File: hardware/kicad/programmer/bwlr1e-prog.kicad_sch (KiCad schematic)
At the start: 46 parts, among them J1 DEBUG, J2 USB_C_Receptacle_USB2.0, J3 RESET, J4 BOOT, Q1 AO3407A, SW1 SW_DIP_x04, SW4 BOOT, SW5 RESET, U1 USBLC6-2P6, U6 CH340E, U7 MCP73831T-2ACI/OT, U8 XC6220B331MR-G

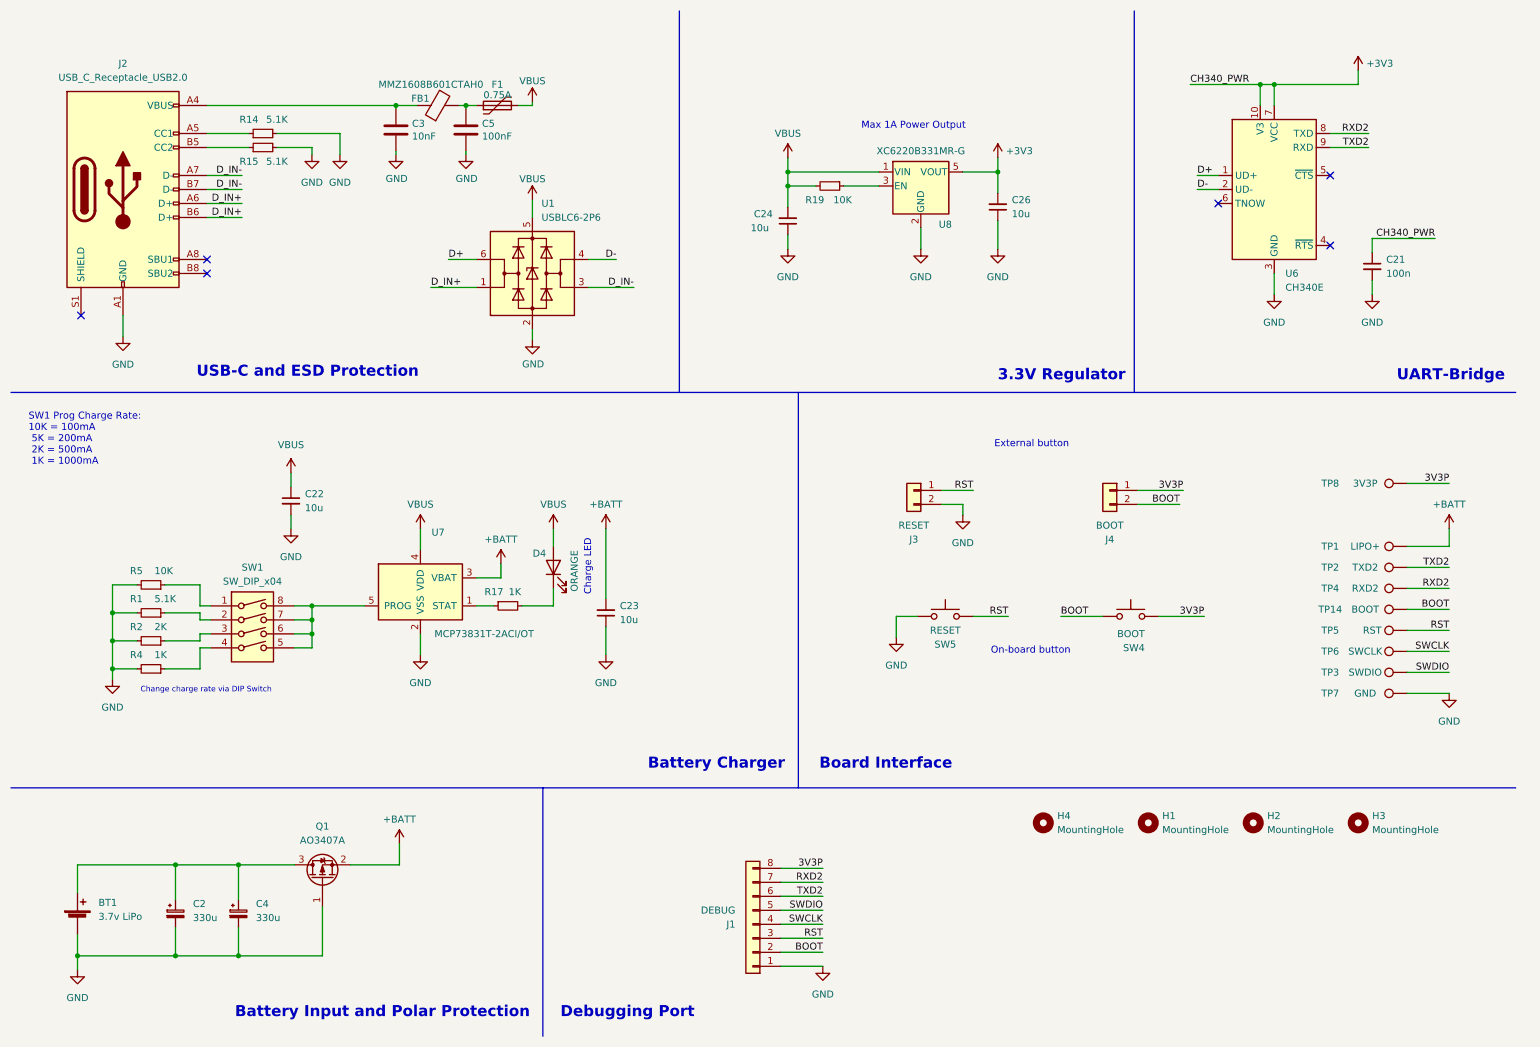
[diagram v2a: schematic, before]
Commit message: fix components value
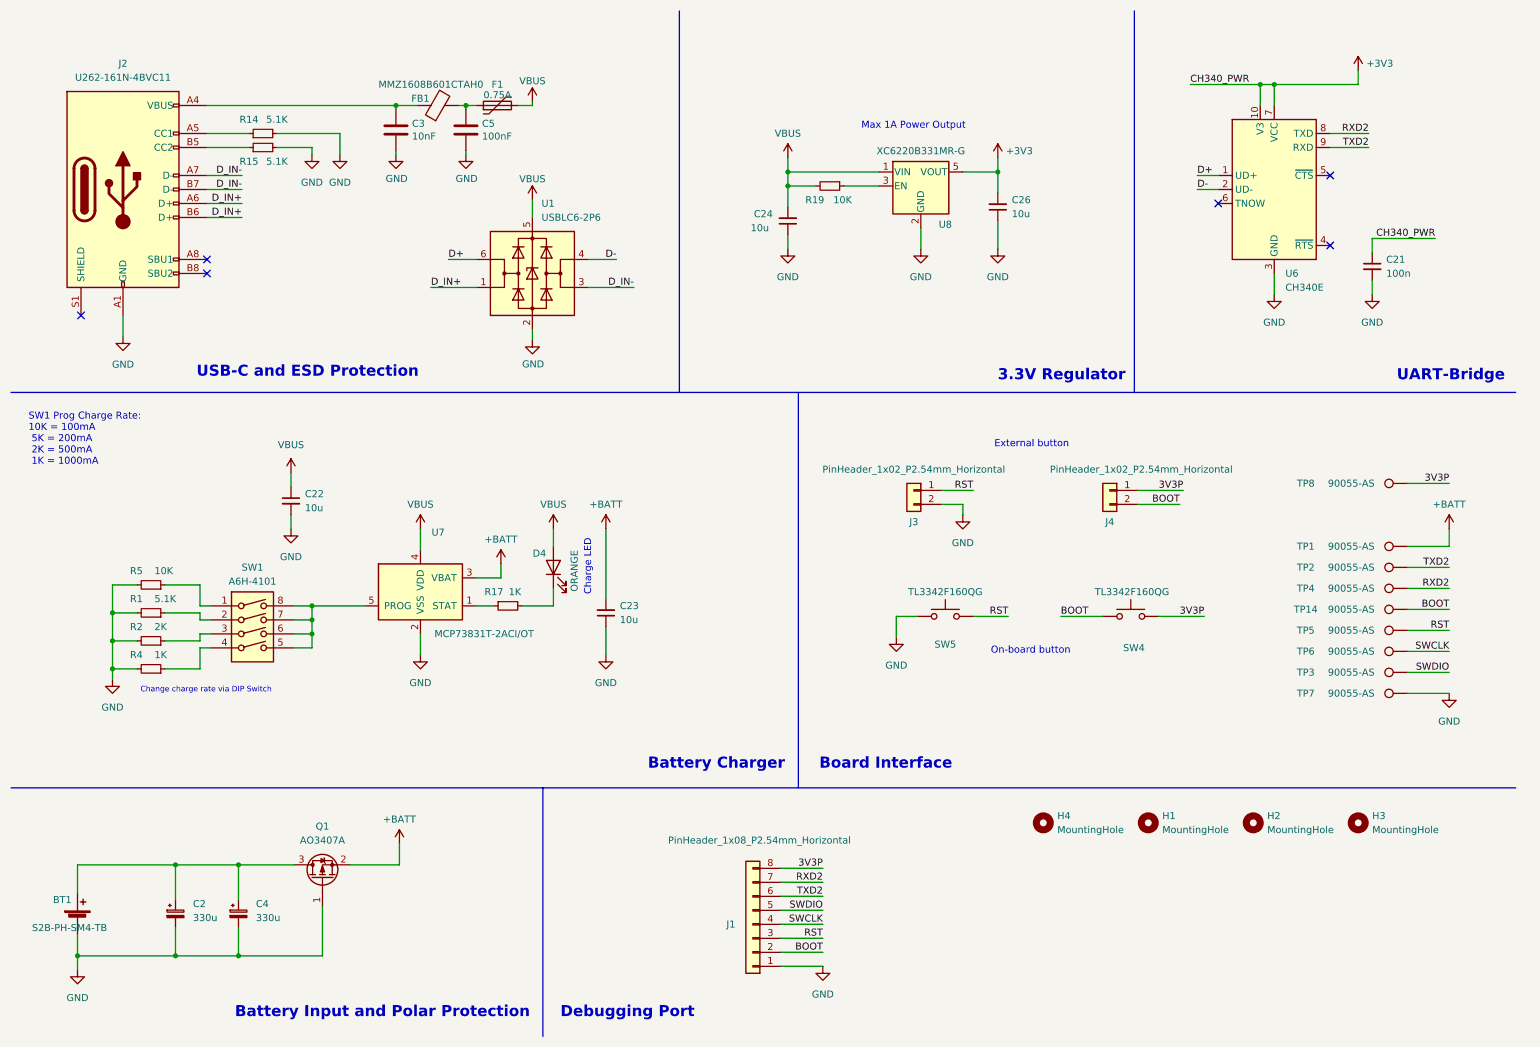
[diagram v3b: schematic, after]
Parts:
- BT1: value 3.7v LiPo -> S2B-PH-SM4-TB
- J1: value DEBUG -> PinHeader_1x08_P2.54mm_Horizontal
- J2: value USB_C_Receptacle_USB2.0 -> U262-161N-4BVC11
- J3: value RESET -> PinHeader_1x02_P2.54mm_Horizontal
- J4: value BOOT -> PinHeader_1x02_P2.54mm_Horizontal
- SW1: value SW_DIP_x04 -> A6H-4101
- SW4: value BOOT -> TL3342F160QG
- SW5: value RESET -> TL3342F160QG
- TP1: value LIPO+ -> 90055-AS
- TP14: value BOOT -> 90055-AS
- TP2: value TXD2 -> 90055-AS
- TP3: value SWDIO -> 90055-AS
- TP4: value RXD2 -> 90055-AS
- TP5: value RST -> 90055-AS
- TP6: value SWCLK -> 90055-AS
- TP7: value GND -> 90055-AS
- TP8: value 3V3P -> 90055-AS
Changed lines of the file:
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@@
   (symbol (lib_id "Connector:TestPoint") (at 265.43 124.46 90) (unit 1)
     (in_bom yes) (on_board yes) (dnp no)
-    (property "Reference" "TP5" (at 251.46 124.46 90)
-      (effects (font (size 1.27 1.27)))
-    )
-    (property "Value" "RST" (at 259.08 124.46 90)
+    (property "Reference" "TP5" (at 247.015 124.46 90)
+      (effects (font (size 1.27 1.27)))
+    )
+    (property "Value" "90055-AS" (at 255.27 124.46 90)
       (effects (font (size 1.27 1.27)))
     )
@@
       (effects (font (size 1.27 1.27)))
     )
-    (property "Value" "RESET" (at 181.61 124.46 0)
+    (property "Value" "TL3342F160QG" (at 181.61 117.475 0)
       (effects (font (size 1.27 1.27)))
     )
@@
       (effects (font (size 1.27 1.27)))
     )
-    (property "Value" "SW_DIP_x04" (at 55.88 115.57 0)
+    (property "Value" "A6H-4101" (at 55.88 115.57 0)
       (effects (font (size 1.27 1.27)))
     )
@@
   (symbol (lib_id "Connector:TestPoint") (at 265.43 109.22 90) (unit 1)
     (in_bom yes) (on_board yes) (dnp no)
-    (property "Reference" "TP1" (at 251.46 109.22 90)
-      (effects (font (size 1.27 1.27)))
-    )
-    (property "Value" "LIPO+" (at 257.81 109.22 90)
+    (property "Reference" "TP1" (at 247.015 109.22 90)
+      (effects (font (size 1.27 1.27)))
+    )
+    (property "Value" "90055-AS" (at 255.27 109.22 90)
       (effects (font (size 1.27 1.27)))
     )
@@
   (symbol (lib_id "Connector:TestPoint") (at 265.43 97.79 90) (unit 1)
     (in_bom yes) (on_board yes) (dnp no)
-    (property "Reference" "TP8" (at 251.46 97.79 90)
-      (effects (font (size 1.27 1.27)))
-    )
-    (property "Value" "3V3P" (at 257.81 97.79 90)
+    (property "Reference" "TP8" (at 247.015 97.79 90)
+      (effects (font (size 1.27 1.27)))
+    )
+    (property "Value" "90055-AS" (at 255.27 97.79 90)
       (effects (font (size 1.27 1.27)))
     )
@@
       (effects (font (size 1.27 1.27)) (justify right))
     )
-    (property "Value" "BOOT" (at 217.805 125.095 0)
+    (property "Value" "TL3342F160QG" (at 222.25 117.475 0)
       (effects (font (size 1.27 1.27)) (justify right))
     )
@@
   (symbol (lib_id "Connector:TestPoint") (at 265.43 135.89 90) (unit 1)
     (in_bom yes) (on_board yes) (dnp no)
-    (property "Reference" "TP7" (at 251.46 135.89 90)
-      (effects (font (size 1.27 1.27)))
-    )
-    (property "Value" "GND" (at 257.81 135.89 90)
+    (property "Reference" "TP7" (at 247.015 135.89 90)
+      (effects (font (size 1.27 1.27)))
+    )
+    (property "Value" "90055-AS" (at 255.27 135.89 90)
       (effects (font (size 1.27 1.27)))
     )
@@
       (effects (font (size 1.27 1.27)))
     )
-    (property "Value" "USB_C_Receptacle_USB2.0" (at 32.385 24.13 0)
+    (property "Value" "U262-161N-4BVC11" (at 32.385 24.13 0)
       (effects (font (size 1.27 1.27)))
     )
@@
   (symbol (lib_id "Connector:TestPoint") (at 265.43 113.03 90) (unit 1)
     (in_bom yes) (on_board yes) (dnp no)
-    (property "Reference" "TP2" (at 251.46 113.03 90)
-      (effects (font (size 1.27 1.27)))
-    )
-    (property "Value" "TXD2" (at 257.81 113.03 90)
+    (property "Reference" "TP2" (at 247.015 113.03 90)
+      (effects (font (size 1.27 1.27)))
+    )
+    (property "Value" "90055-AS" (at 255.27 113.03 90)
       (effects (font (size 1.27 1.27)))
     )
@@
   (symbol (lib_id "Connector:TestPoint") (at 265.43 132.08 90) (unit 1)
     (in_bom yes) (on_board yes) (dnp no)
-    (property "Reference" "TP3" (at 251.46 132.08 90)
-      (effects (font (size 1.27 1.27)))
-    )
-    (property "Value" "SWDIO" (at 257.81 132.08 90)
+    (property "Reference" "TP3" (at 247.015 132.08 90)
+      (effects (font (size 1.27 1.27)))
+    )
+    (property "Value" "90055-AS" (at 255.27 132.08 90)
       (effects (font (size 1.27 1.27)))
     )
@@
   (symbol (lib_id "Connector_Generic:Conn_01x02") (at 175.895 99.06 0) (mirror y) (unit 1)
     (in_bom yes) (on_board yes) (dnp no)
-    (property "Reference" "J3" (at 175.895 107.95 0)
-      (effects (font (size 1.27 1.27)))
-    )
-    (property "Value" "RESET" (at 175.895 105.41 0)
+    (property "Reference" "J3" (at 175.895 104.775 0)
+      (effects (font (size 1.27 1.27)))
+    )
+    (property "Value" "PinHeader_1x02_P2.54mm_Horizontal" (at 175.895 95.25 0)
       (effects (font (size 1.27 1.27)))
     )
@@
   )
   (symbol (lib_id "Device:Battery_Cell") (at 24.13 177.165 0) (unit 1)
-    (in_bom yes) (on_board yes) (dnp no) (fields_autoplaced)
-    (property "Reference" "BT1" (at 27.94 173.8629 0)
-      (effects (font (size 1.27 1.27)) (justify left))
-    )
-    (property "Value" "3.7v LiPo" (at 27.94 176.4029 0)
+    (in_bom yes) (on_board yes) (dnp no)
+    (property "Reference" "BT1" (at 19.685 173.355 0)
+      (effects (font (size 1.27 1.27)) (justify left))
+    )
+    (property "Value" "S2B-PH-SM4-TB" (at 15.875 178.435 0)
       (effects (font (size 1.27 1.27)) (justify left))
     )
@@
       (effects (font (size 1.27 1.27)) (justify left))
     )
-    (property "Value" "DEBUG" (at 143.51 175.26 0)
+    (property "Value" "PinHeader_1x08_P2.54mm_Horizontal" (at 164.465 162.56 0)
       (effects (font (size 1.27 1.27)) (justify left))
     )
@@
   (symbol (lib_id "Connector:TestPoint") (at 265.43 128.27 90) (unit 1)
     (in_bom yes) (on_board yes) (dnp no)
-    (property "Reference" "TP6" (at 251.46 128.27 90)
-      (effects (font (size 1.27 1.27)))
-    )
-    (property "Value" "SWCLK" (at 257.81 128.27 90)
+    (property "Reference" "TP6" (at 247.015 128.27 90)
+      (effects (font (size 1.27 1.27)))
+    )
+    (property "Value" "90055-AS" (at 255.27 128.27 90)
       (effects (font (size 1.27 1.27)))
     )
@@
   (symbol (lib_id "Connector_Generic:Conn_01x02") (at 211.455 99.06 0) (mirror y) (unit 1)
     (in_bom yes) (on_board yes) (dnp no)
-    (property "Reference" "J4" (at 211.455 107.95 0)
-      (effects (font (size 1.27 1.27)))
-    )
-    (property "Value" "BOOT" (at 211.455 105.41 0)
+    (property "Reference" "J4" (at 211.455 104.775 0)
+      (effects (font (size 1.27 1.27)))
+    )
+    (property "Value" "PinHeader_1x02_P2.54mm_Horizontal" (at 217.17 95.25 0)
       (effects (font (size 1.27 1.27)))
     )
@@
   (symbol (lib_id "Connector:TestPoint") (at 265.43 116.84 90) (unit 1)
     (in_bom yes) (on_board yes) (dnp no)
-    (property "Reference" "TP4" (at 251.46 116.84 90)
-      (effects (font (size 1.27 1.27)))
-    )
-    (property "Value" "RXD2" (at 257.81 116.84 90)
+    (property "Reference" "TP4" (at 247.015 116.84 90)
+      (effects (font (size 1.27 1.27)))
+    )
+    (property "Value" "90055-AS" (at 255.27 116.84 90)
       (effects (font (size 1.27 1.27)))
     )
@@
   (symbol (lib_id "Connector:TestPoint") (at 265.43 120.65 90) (unit 1)
     (in_bom yes) (on_board yes) (dnp no)
-    (property "Reference" "TP14" (at 251.46 120.65 90)
-      (effects (font (size 1.27 1.27)))
-    )
-    (property "Value" "BOOT" (at 257.81 120.65 90)
-      (effects (font (size 1.27 1.27)))
-    )
+    (property "Reference" "TP14" (at 247.015 120.65 90)
+      (effects (font (size 1.27 1.27)))
+    )
+    (property "Value" "90055-AS" (at 255.27 120.65 90)
+      (effects (font (size 1.27 1.27)))
+    )

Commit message: add usb-c receptacle
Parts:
- D4: Part Description (none) -> Orange 2V 25mA; Part Number Orange 2V 25mA -> (none)
- J2: footprint Teapot:USB_C_Receptacle_XKB_U262-16XN-4BVC11 -> bwlr1e_prog:USB_C_Receptacle_XKB_U262-16XN-4BVC11
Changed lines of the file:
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@@
       (effects (font (size 1.27 1.27)) hide)
     )
-    (property "Part Number" "Orange 2V 25mA" (at 110.49 113.03 90)
+    (property "Part Description" "Orange 2V 25mA" (at 110.49 113.03 90)
       (effects (font (size 1.27 1.27)) hide)
     )
@@
       (effects (font (size 1.27 1.27)))
     )
-    (property "Footprint" "Teapot:USB_C_Receptacle_XKB_U262-16XN-4BVC11" (at 36.195 44.45 0)
-      (effects (font (size 1.27 1.27)) hide)
-    )
+    (property "Footprint" "bwlr1e_prog:USB_C_Receptacle_XKB_U262-16XN-4BVC11" (at 36.195 44.45 0)
+      (effects (font (size 1.27 1.27)) hide)
+    )

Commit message: fix incorrect resistor desc
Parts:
- R14, R15: Part Description Resistor 5.1K 1% 100mW -> Resistor 5.1K 1% 62.5mW
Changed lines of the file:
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@@
       (effects (font (size 1.27 1.27)) hide)
     )
-    (property "Part Description" "Resistor 5.1K 1% 100mW" (at 57.785 36.83 90)
+    (property "Part Description" "Resistor 5.1K 1% 62.5mW" (at 57.785 36.83 90)
       (effects (font (size 1.27 1.27)) hide)
     )
@@
       (effects (font (size 1.27 1.27)) hide)
     )
-    (property "Part Description" "Resistor 5.1K 1% 100mW" (at 57.785 34.29 90)
-      (effects (font (size 1.27 1.27)) hide)
-    )
+    (property "Part Description" "Resistor 5.1K 1% 62.5mW" (at 57.785 34.29 90)
+      (effects (font (size 1.27 1.27)) hide)
+    )

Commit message: rename value
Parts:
- C3: value 10nF -> 10n
- C5: value 100nF -> 100n
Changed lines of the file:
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@@
       (effects (font (size 1.27 1.27)) (justify left))
     )
-    (property "Value" "100nF" (at 97.536 34.798 0)
+    (property "Value" "100n" (at 97.536 34.798 0)
       (effects (font (size 1.27 1.27)) (justify left))
     )
@@
       (effects (font (size 1.27 1.27)) (justify left))
     )
-    (property "Value" "10nF" (at 84.836 34.798 0)
-      (effects (font (size 1.27 1.27)) (justify left))
-    )
+    (property "Value" "10n" (at 84.836 34.798 0)
+      (effects (font (size 1.27 1.27)) (justify left))
+    )

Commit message: re-annotate
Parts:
- renumbered C2 to C1, C4 to C2, C22 to C3, C3 to C4, C23 to C6, C24 to C7, C26 to C8, C21 to C9, D4 to D1, H4 to H1, H1 to H2, H2 to H3, H3 to H4, J2 to J1, J1 to J2, R5 to R1, R1 to R2, R2 to R3, R14 to R5, R15 to R6, R17 to R7, R19 to R8, SW5 to SW2, SW4 to SW3, TP8 to TP1, TP1 to TP2, TP2 to TP3, TP14 to TP5, TP5 to TP6, TP6 to TP7, TP3 to TP8, TP7 to TP9, U7 to U1, U1 to U2, U8 to U3, U6 to U4
